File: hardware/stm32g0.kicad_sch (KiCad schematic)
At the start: 31 parts, among them J401 TagConnect, Q401 AO3400A, Q402 AO3400A, SW1 RESET, U401 STM32G071RBTx, Y401 12MHz

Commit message: Fix SiC437 footprint and LCSC field error
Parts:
- C401, C402, C403: LCSC ID (none) -> C307331; LCSC Part C307331 -> (none)
- C404: LCSC ID (none) -> C96446; LCSC Part C96446 -> (none)
- C405, C406: LCSC ID (none) -> C1554; LCSC Part C1554 -> (none)
- D401, D402, D403: LCSC ID (none) -> C2290; LCSC Part C2290 -> (none)
- Q401, Q402: LCSC ID (none) -> AO3400A; LCSC Part AO3400A -> (none)
- R401, R402, R403, R408, R409: LCSC ID (none) -> C25794; LCSC Part C25794 -> (none)
- R404, R405, R406, R410, R411: LCSC ID (none) -> C137947; LCSC Part C137947 -> (none)
- R407, R413, R414: LCSC ID (none) -> C25744; LCSC Part C25744 -> (none)
- R412, R415, R416: LCSC ID (none) -> C25905; LCSC Part C25905 -> (none)
- SW1: LCSC ID (none) -> C318884; LCSC Part C318884 -> (none)
- U401: LCSC ID (none) -> C432213; LCSC Part C432213 -> (none)
- Y401: LCSC ID (none) -> C9002; LCSC Part C9002 -> (none)
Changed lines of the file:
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@@
 			)
 		)
-		(property "LCSC Part" "C137947"
+		(property "LCSC ID" "C137947"
 			(at 181.61 33.02 0)
 			(effects
@@
 			)
 		)
-		(property "LCSC Part" "C9002"
+		(property "LCSC ID" "C9002"
 			(at 240.03 143.51 0)
 			(effects
@@
 			)
 		)
-		(property "LCSC Part" "C1554"
+		(property "LCSC ID" "C1554"
 			(at 247.65 148.59 0)
 			(effects
@@
 			)
 		)
-		(property "LCSC Part" "AO3400A"
+		(property "LCSC ID" "AO3400A"
 			(at 242.57 90.17 0)
 			(effects
@@
 			)
 		)
-		(property "LCSC Part" "C318884"
+		(property "LCSC ID" "C318884"
 			(at 186.69 151.13 0)
 			(effects
@@
 			)
 		)
-		(property "LCSC Part" "C2290"
+		(property "LCSC ID" "C2290"
 			(at 48.26 107.95 0)
 			(effects
@@
 			)
 		)
-		(property "LCSC Part" "C25905"
+		(property "LCSC ID" "C25905"
 			(at 240.03 110.49 0)
 			(effects
@@
 			)
 		)
-		(property "LCSC Part" "C25794"
+		(property "LCSC ID" "C25794"
 			(at 186.69 27.94 0)
 			(effects
@@
 			)
 		)
-		(property "LCSC Part" "C25744"
+		(property "LCSC ID" "C25744"
 			(at 199.39 144.78 0)
 			(effects
@@
 			)
 		)
-		(property "LCSC Part" "C432213"
+		(property "LCSC ID" "C432213"
 			(at 88.9 87.63 0)
 			(effects
@@
 			)
 		)
-		(property "LCSC Part" "C307331"
+		(property "LCSC ID" "C307331"
 			(at 116.84 33.02 0)
 			(effects
@@
 			)
 		)
-		(property "LCSC Part" "C1554"
+		(property "LCSC ID" "C1554"
 			(at 232.41 148.59 0)
 			(effects
@@
 			)
 		)
-		(property "LCSC Part" "C307331"
+		(property "LCSC ID" "C307331"
 			(at 96.52 33.02 0)
 			(effects
@@
 			)
 		)
-		(property "LCSC Part" "C96446"
+		(property "LCSC ID" "C96446"
 			(at 127 33.02 0)
 			(effects
@@
 			)
 		)
-		(property "LCSC Part" "C25794"
+		(property "LCSC ID" "C25794"
 			(at 217.17 53.34 0)
 			(effects
@@
 			)
 		)
-		(property "LCSC Part" "C25794"
+		(property "LCSC ID" "C25794"
 			(at 259.08 27.94 0)
 			(effects
@@
 			)
 		)
-		(property "LCSC Part" "C137947"
+		(property "LCSC ID" "C137947"
 			(at 254 33.02 0)
 			(effects
@@
 			)
 		)
-		(property "LCSC Part" "C25794"
+		(property "LCSC ID" "C25794"
 			(at 259.08 53.34 0)
 			(effects
@@
 			)
 		)
-		(property "LCSC Part" "C25794"
+		(property "LCSC ID" "C25794"
 			(at 217.17 27.94 0)
 			(effects
@@
 			)
 		)
+		(property "LCSC ID" ""
+			(at 53.34 170.18 0)
+			(effects
+				(font
+					(size 1.27 1.27)
+				)
+				(hide yes)
+			)
+		)
 		(pin "6"
 		)
@@
 			)
 		)
-		(property "LCSC Part" "C307331"
+		(property "LCSC ID" "C307331"
 			(at 106.68 33.02 0)
 			(effects
@@
 			)
 		)
-		(property "LCSC Part" "C137947"
+		(property "LCSC ID" "C137947"
 			(at 212.09 58.42 0)
 			(effects
@@
 			)
 		)
-		(property "LCSC Part" "C25905"
+		(property "LCSC ID" "C25905"
 			(at 59.69 107.95 0)
 			(effects
@@
 			)
 		)
-		(property "LCSC Part" "C2290"
+		(property "LCSC ID" "C2290"
 			(at 240.03 101.6 0)
 			(effects
@@
 			)
 		)
-		(property "LCSC Part" "AO3400A"
+		(property "LCSC ID" "AO3400A"
 			(at 190.5 90.17 0)
 			(effects
@@
 			)
 		)
-		(property "LCSC Part" "C137947"
+		(property "LCSC ID" "C137947"
 			(at 212.09 33.02 0)
 			(effects
@@
 			)
 		)
-		(property "LCSC Part" "C2290"
+		(property "LCSC ID" "C2290"
 			(at 187.96 101.6 0)
 			(effects
@@
 			)
 		)
-		(property "LCSC Part" "C25905"
+		(property "LCSC ID" "C25905"
 			(at 187.96 110.49 0)
 			(effects
@@
 			)
 		)
-		(property "LCSC Part" "C25744"
+		(property "LCSC ID" "C25744"
 			(at 193.04 96.52 0)
 			(effects
@@
 			)
 		)
-		(property "LCSC Part" "C25744"
+		(property "LCSC ID" "C25744"
 			(at 245.11 96.52 0)
 			(effects
@@
 			)
 		)
-		(property "LCSC Part" "C137947"
+		(property "LCSC ID" "C137947"
 			(at 254 58.42 0)
 			(effects

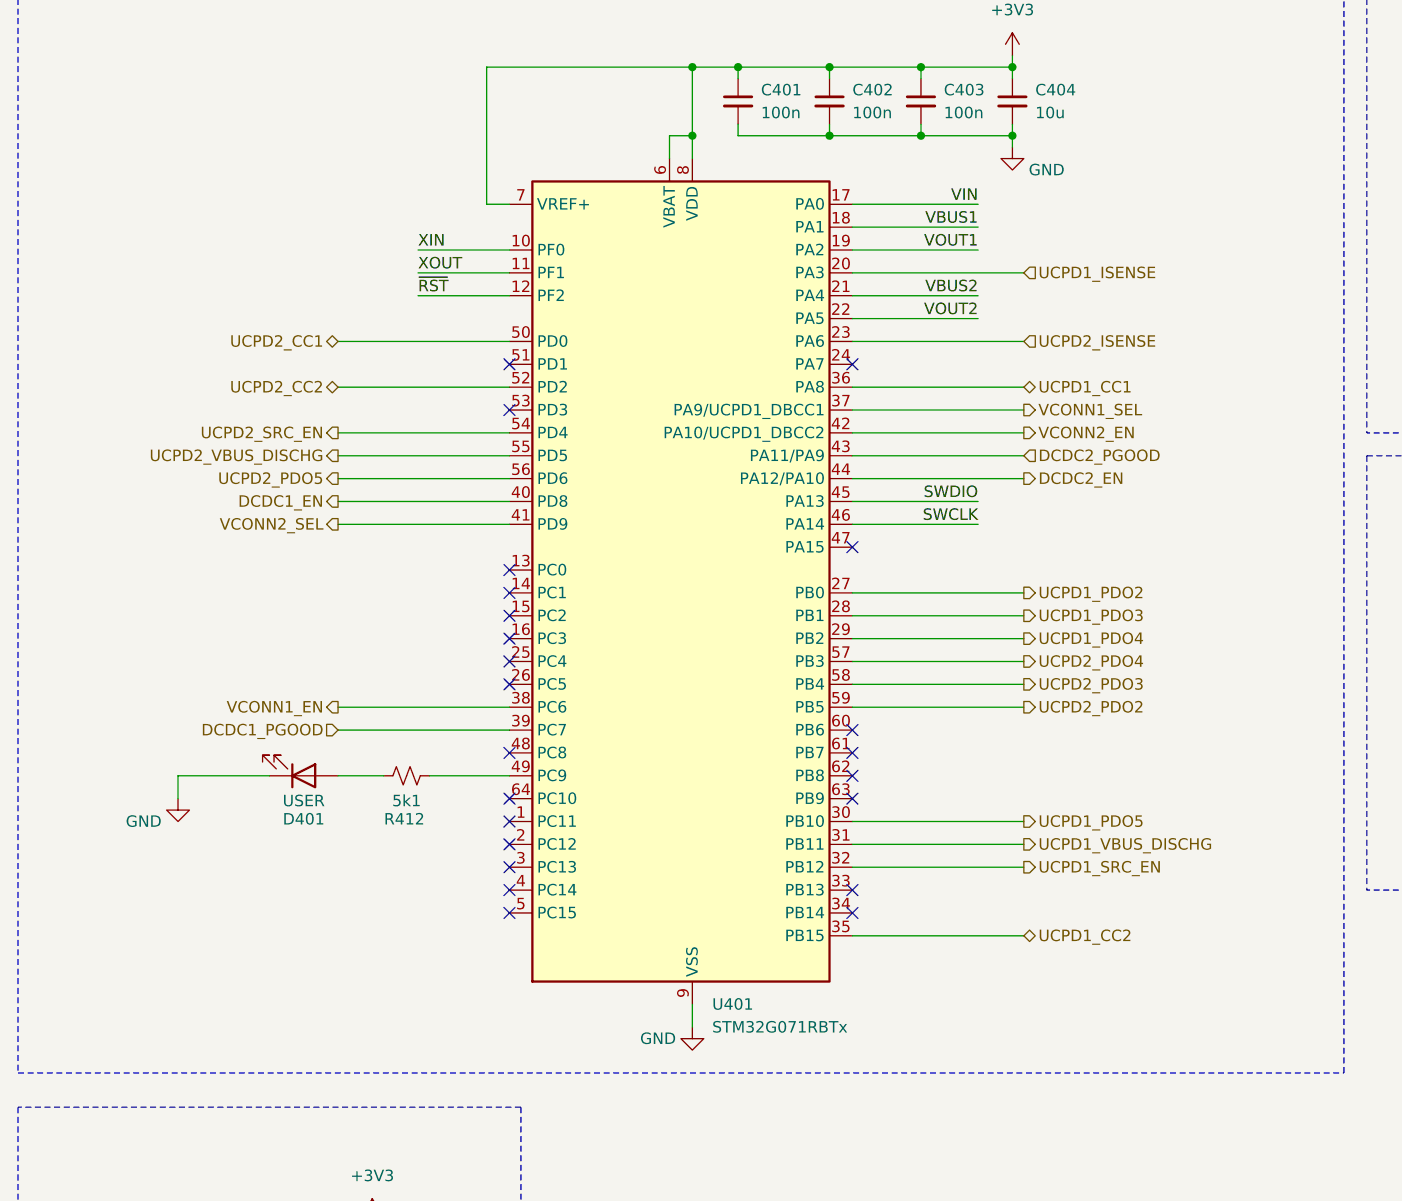
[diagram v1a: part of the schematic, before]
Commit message: change to C8U3 variant
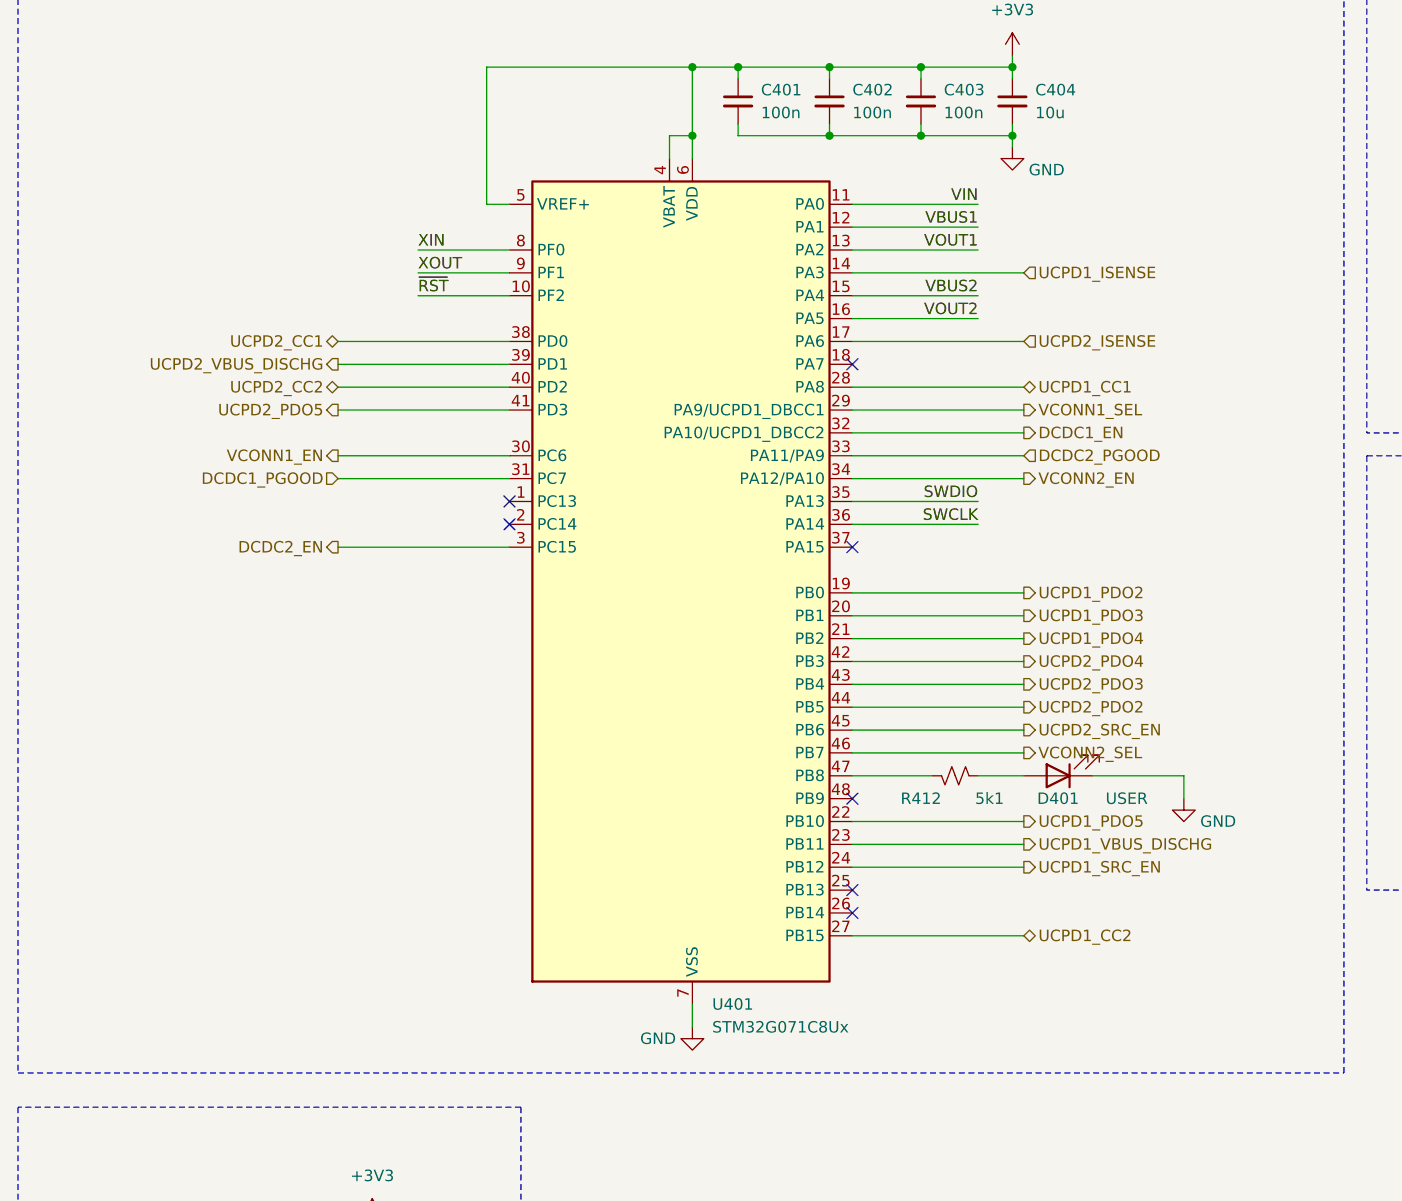
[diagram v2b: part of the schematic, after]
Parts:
- removed U401: STM32G071RBTx, Package_QFP:LQFP-64_10x10mm_P0.5mm, symbol MCU_ST_STM32G0:STM32G071RBTx
- added U401: STM32G071C8Ux, Package_DFN_QFN:QFN-48-1EP_7x7mm_P0.5mm_EP5.6x5.6mm, symbol MCU_ST_STM32G0:STM32G071C8Ux
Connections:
- net +3V3: now also U401.4 (VBAT), U401.5 (VREF+), U401.6 (VDD)
- net DCDC1_EN: now also U401.32 (PA10/UCPD1_DBCC2)
- net DCDC1_PGOOD: now also U401.31 (PC7)
- net DCDC2_EN: now also U401.3 (PC15)
- net DCDC2_PGOOD: now also U401.33 (PA11/PA9)
- net GND: now also U401.49 (VSS), U401.7 (VSS)
- net SWCLK: now also U401.36 (PA14)
- net SWDIO: now also U401.35 (PA13)
- net UCPD1_CC1: now also U401.28 (PA8)
- net UCPD1_CC2: now also U401.27 (PB15)
- net UCPD1_ISENSE: now also U401.14 (PA3)
- net UCPD1_PDO2: now also U401.19 (PB0)
- net UCPD1_PDO3: now also U401.20 (PB1)
- net UCPD1_PDO4: now also U401.21 (PB2)
- net UCPD1_PDO5: now also U401.22 (PB10)
- net UCPD1_SRC_EN: now also U401.24 (PB12)
- net UCPD1_VBUS_DISCHG: now also U401.23 (PB11)
- net UCPD2_CC1: now also U401.38 (PD0)
- net UCPD2_CC2: now also U401.40 (PD2)
- net UCPD2_ISENSE: now also U401.17 (PA6)
- net UCPD2_PDO2: now also U401.44 (PB5)
- net UCPD2_PDO3: now also U401.43 (PB4)
- net UCPD2_PDO4: now also U401.42 (PB3)
- net UCPD2_PDO5: now also U401.41 (PD3)
- net UCPD2_SRC_EN: now also U401.45 (PB6)
- net UCPD2_VBUS_DISCHG: now also U401.39 (PD1)
- net VBUS1: now also U401.12 (PA1)
- net VBUS2: now also U401.15 (PA4)
- net VCONN1_EN: now also U401.30 (PC6)
- net VCONN1_SEL: now also U401.29 (PA9/UCPD1_DBCC1)
- net VCONN2_EN: now also U401.34 (PA12/PA10)
- net VCONN2_SEL: now also U401.46 (PB7)
- net VIN: now also U401.11 (PA0)
- net VOUT1: now also U401.13 (PA2)
- net VOUT2: now also U401.16 (PA5)
- net XIN: now also U401.8 (PF0)
- net XOUT: now also U401.9 (PF1)
- net ~{RST}: now also U401.10 (PF2)
- net at R412.1: now also U401.47 (PB8)
- no-connect marks 24 -> 8
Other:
- moved on the sheet: D401, R412

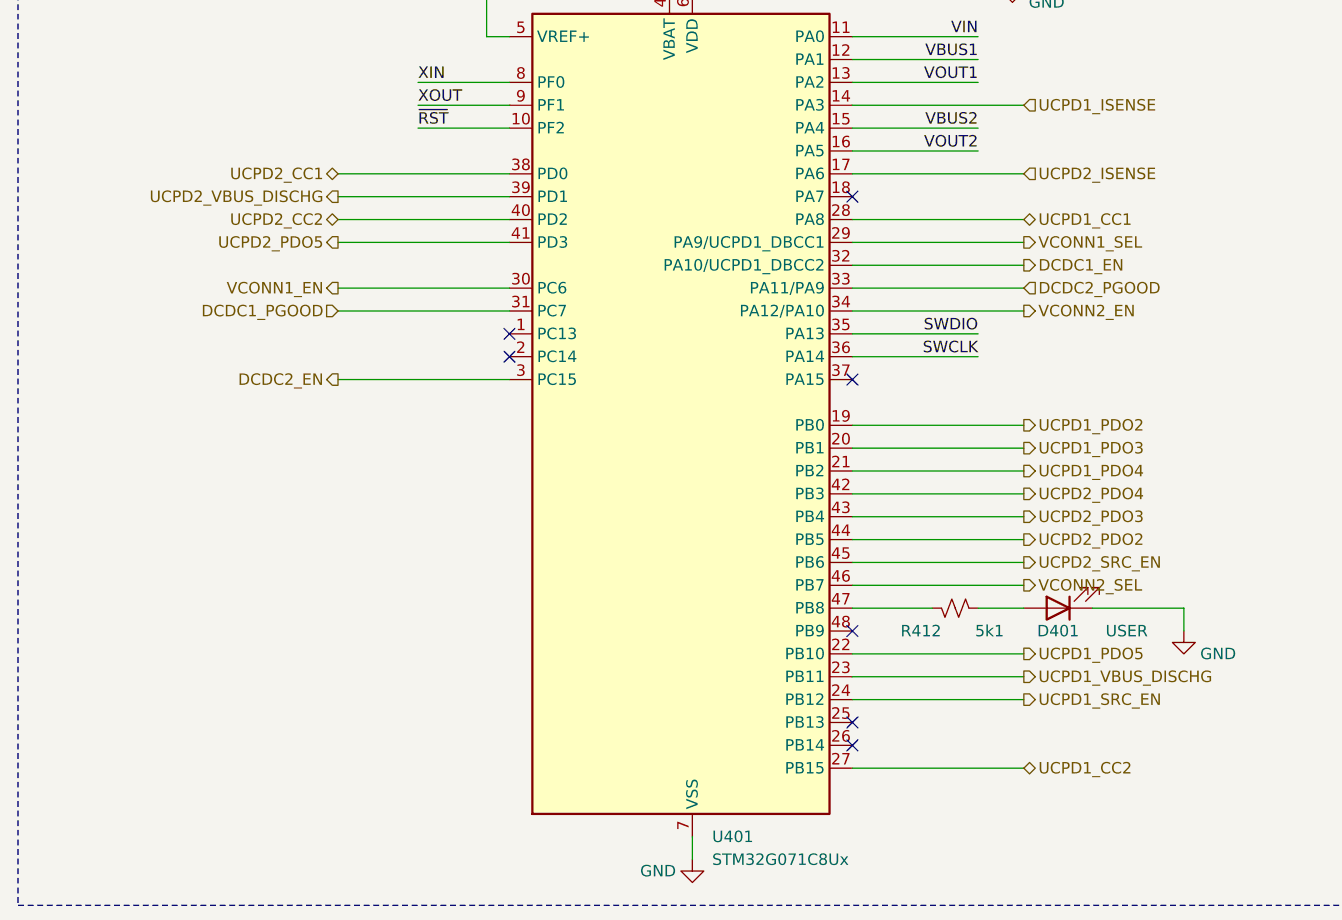
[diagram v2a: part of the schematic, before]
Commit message: fix pinout issues hw rev 1
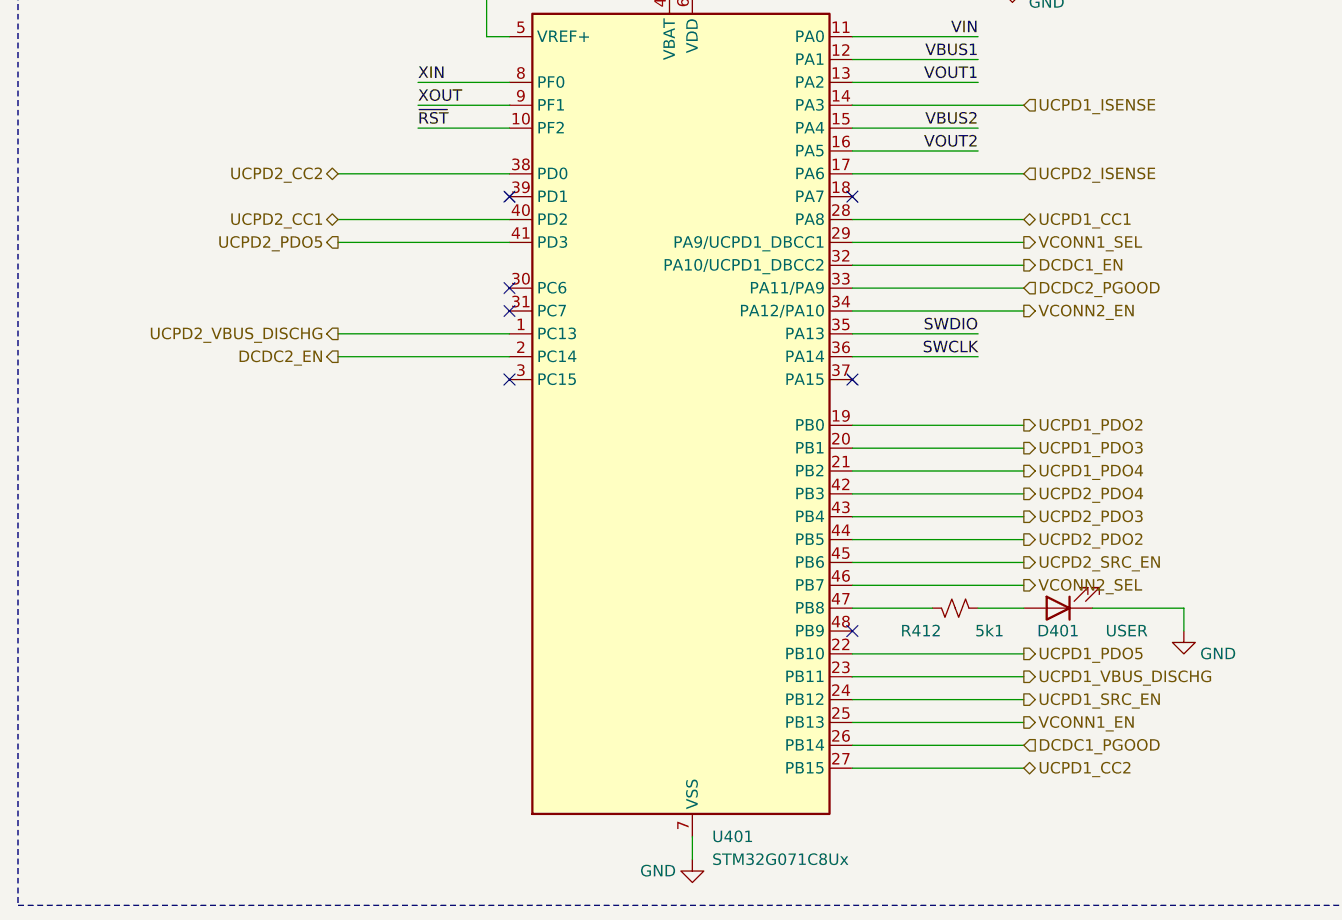
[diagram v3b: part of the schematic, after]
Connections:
- net DCDC1_PGOOD: now also U401.26 (PB14); no longer U401.31 (PC7)
- net DCDC2_EN: now also U401.2 (PC14); no longer U401.3 (PC15)
- net UCPD2_CC1: now also U401.40 (PD2); no longer U401.38 (PD0)
- net UCPD2_CC2: now also U401.38 (PD0); no longer U401.40 (PD2)
- net UCPD2_VBUS_DISCHG: now also U401.1 (PC13); no longer U401.39 (PD1)
- net VCONN1_EN: now also U401.25 (PB13); no longer U401.30 (PC6)
